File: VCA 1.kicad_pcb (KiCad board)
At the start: 2 copper layers, 171.3 x 128.5 mm, 87 parts, among them J1 Eurorack 2x8hs, J10 CV2, J11 IN2, J12 IN 1x8h, J13 OUT1, J14 OUT2, J15 IN 1x8s, J2 OUT 1x3s, J3 CV 1x9s, J5 CV 1x9h, J6 OUT 1x3h, J8 CV1, J9 IN1, Q1 2N3904, Q2 2N3904, U1 TL074, U2 AS2164

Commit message: Updated trim pot footprints
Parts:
- RV10, RV7, RV8, RV9: footprint Potentiometer_THT:Potentiometer_Bourns_3296W_Vertical -> Potentiometer_THT:Potentiometer_Bourns_3296X_Horizontal
- moved RV7 6.50 mm to (66.7, 55.6), turned to 180 degrees
- moved R16 5.02 mm to (55.1, 45.5), turned to 0 degrees
- moved RV8 3.52 mm to (66.7, 48.2), turned to 180 degrees
- moved RV10 2.66 mm to (62.2, 41.7), turned to -90 degrees
- moved RV9 0.50 mm to (54.0, 41.7), turned to -90 degrees
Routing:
- net Net-(R7-Pad1): track 4.29 -> 40.7 mm
- net Net-(R16-Pad1): track 5.23 -> 32.1 mm
- net -12v: track 185.4 -> 174.1 mm
- net Net-(R6-Pad1): track 4.33 -> 14.9 mm
- net Net-(R15-Pad1): track 4.98 -> 8.18 mm
- net GND: vias 9 -> 10
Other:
- board text added: "V 1.4"
- board text removed: "V 1.3"

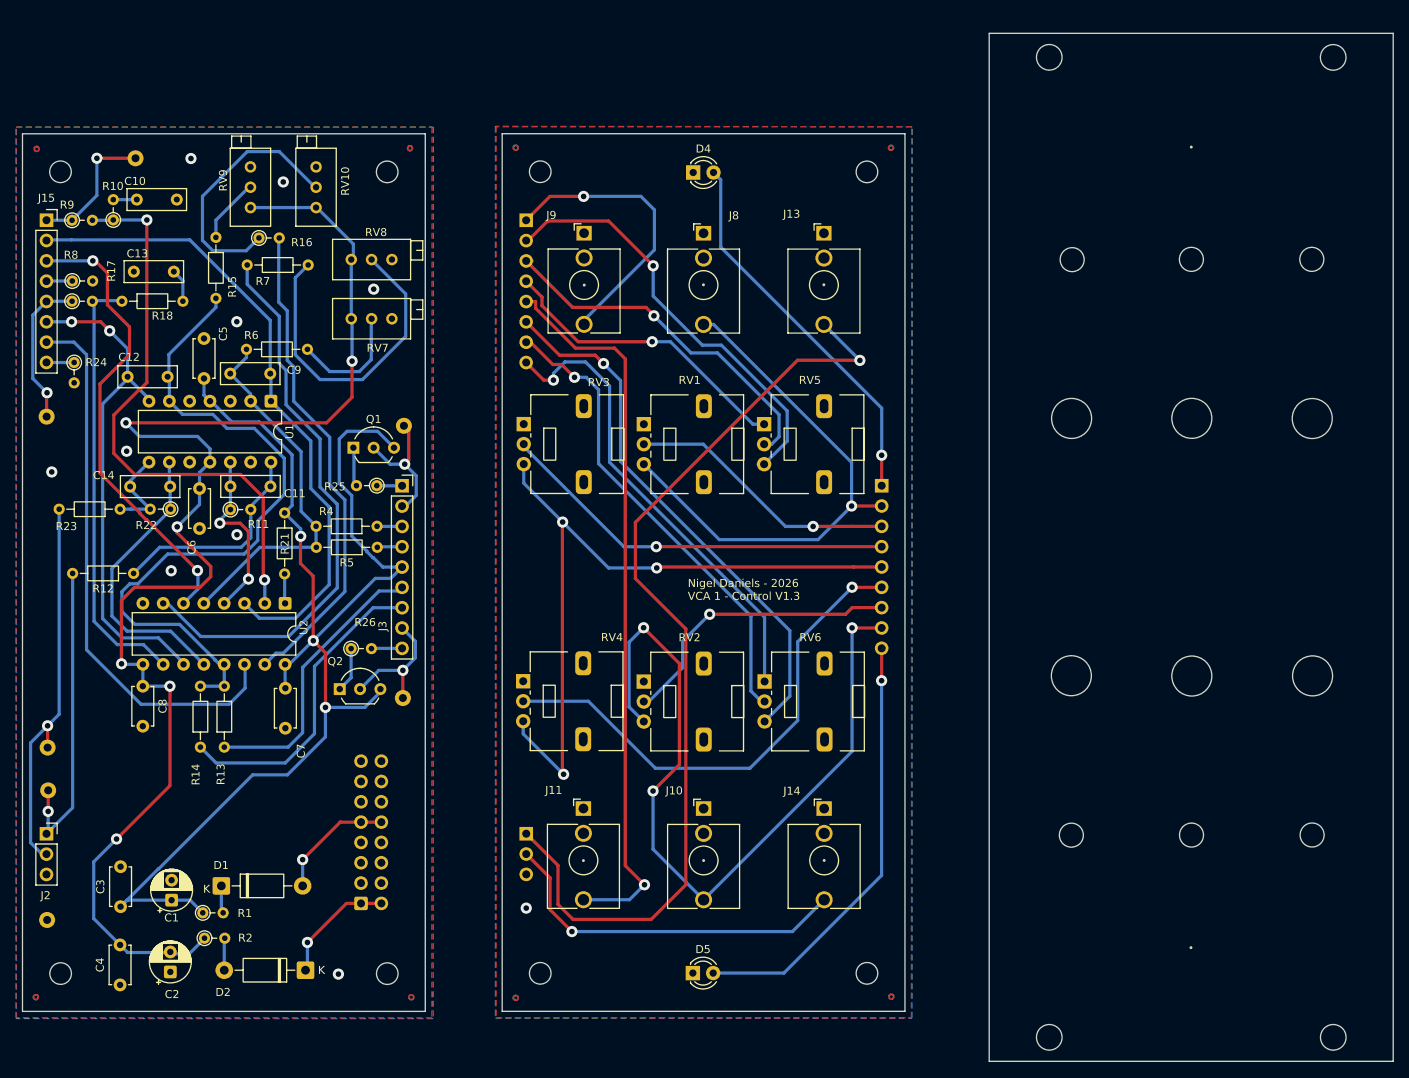
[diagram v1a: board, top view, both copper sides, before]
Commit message: Created custom AS2164 symbol, updated schematic, pcb and readme.
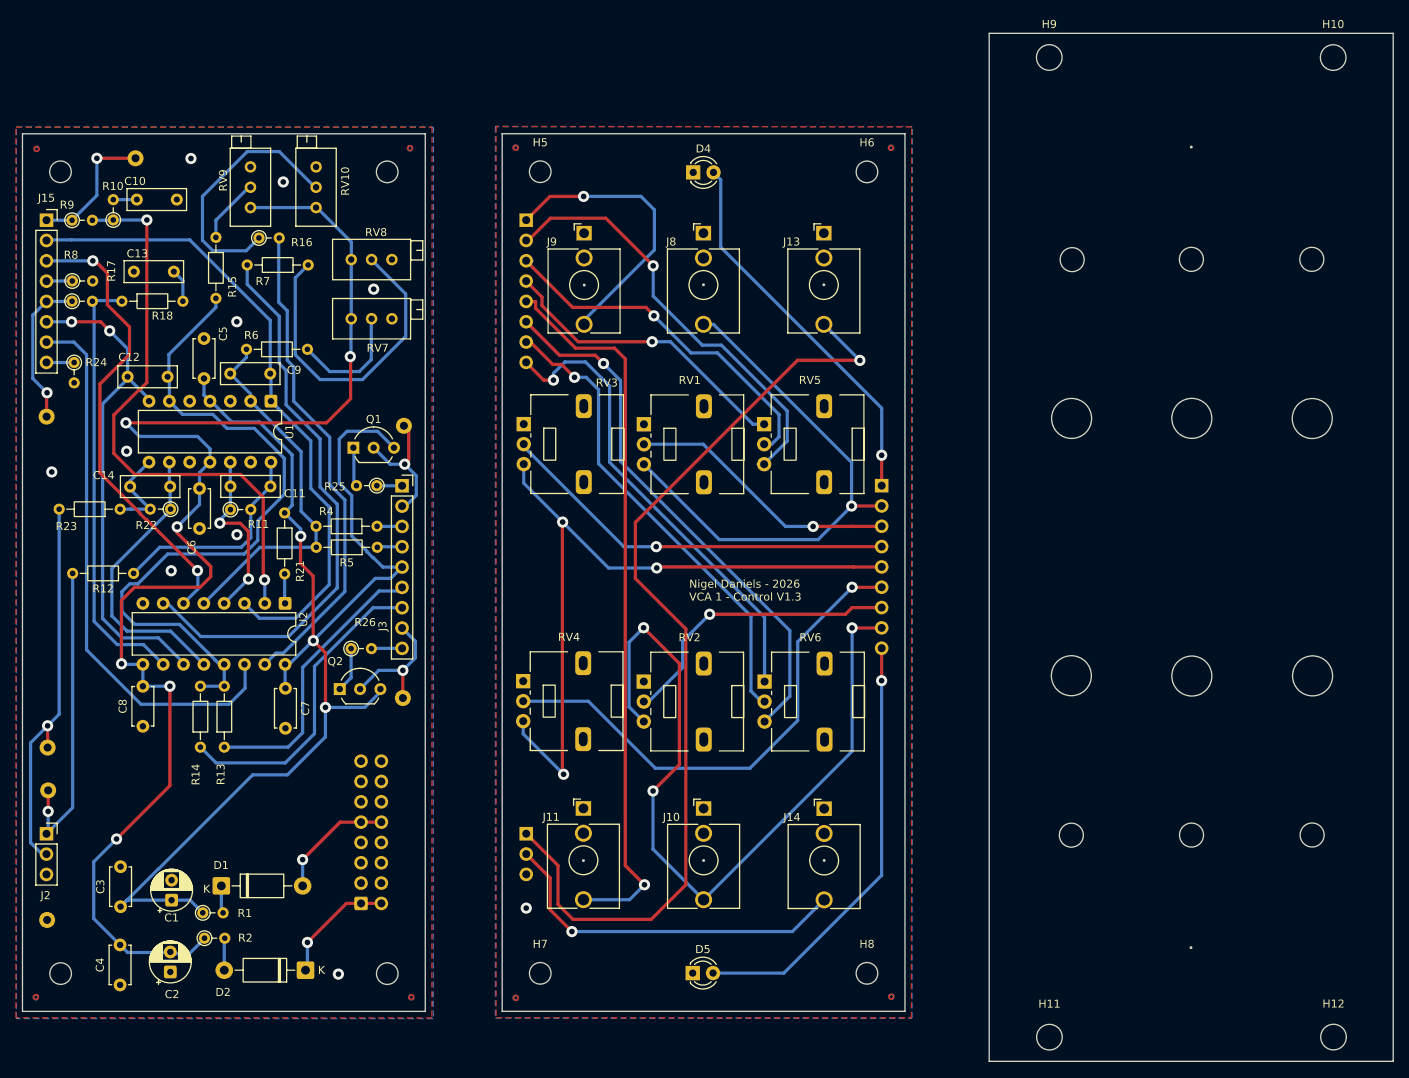
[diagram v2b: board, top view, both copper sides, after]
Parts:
- moved H7 40.8 mm to (90.3, 137.4)
- moved H8 40.8 mm to (131.1, 137.4)
- moved H12 35.5 mm to (189.4, 145.4)
- moved H11 35.5 mm to (153.9, 145.4)
- moved C8 5.01 mm to (40.6, 106.5), turned to 90 degrees
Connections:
- C8 pad 1: -12v -> GND
- C8 pad 2: GND -> -12v

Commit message: New simulation, updated design after breadboard test.
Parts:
- added R19: 390R, Resistor_THT:R_Axial_DIN0204_L3.6mm_D1.6mm_P2.54mm_Vertical, F.Cu at (34.4, 48.4)
- added R20: 390R, Resistor_THT:R_Axial_DIN0204_L3.6mm_D1.6mm_P2.54mm_Vertical, F.Cu at (53.3, 101.7)
- R24, R8: value 2K2 -> 3K3
- RV5, RV6: value 10K B -> 1K B
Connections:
- U2 pad 14: Net-(J15-Pin_7) -> Net-(U2D-CV)
- U2 pad 6: Net-(J15-Pin_3) -> Net-(U2B-CV)
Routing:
- net Net-(J15-Pin_3): track 58.4 -> 3.26 mm, vias 2 -> 0
- net Net-(U2B-CV): track 0.00 -> 54.5 mm, vias 0 -> 2
- net Net-(J15-Pin_7): track 69.0 -> 65.5 mm
- net Net-(U2D-CV): track 0.00 -> 3.03 mm

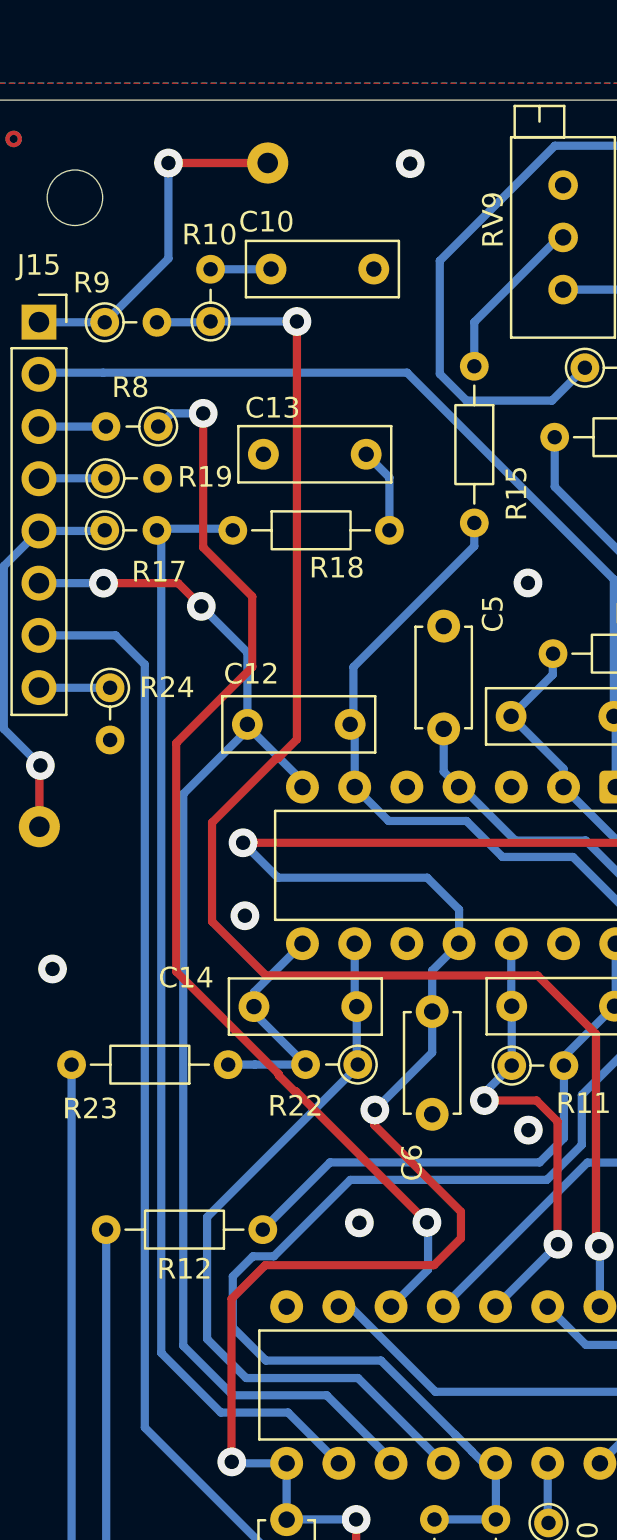
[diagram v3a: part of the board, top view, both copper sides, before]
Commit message: Updated curve values to match breadboard
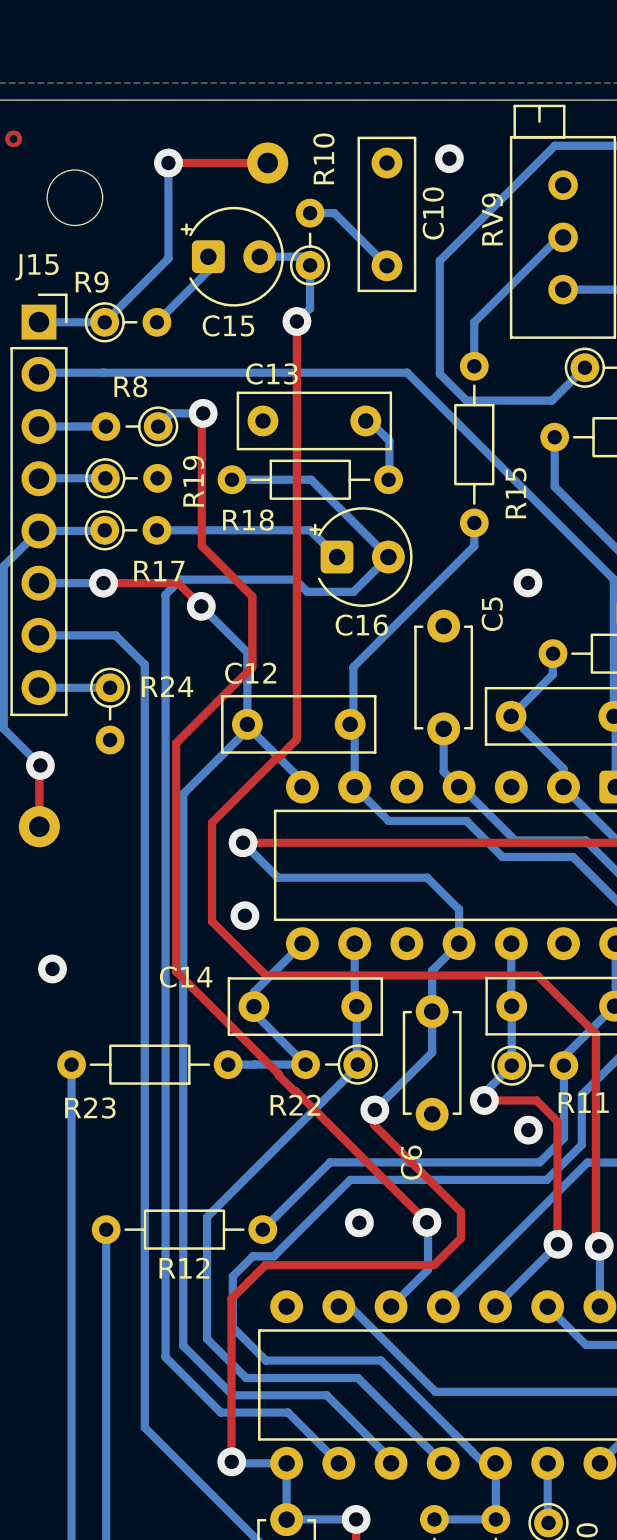
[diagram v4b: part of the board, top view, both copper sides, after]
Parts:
- added C15: 10uF t, Capacitor_THT:CP_Radial_Tantal_D4.5mm_P2.50mm, F.Cu at (36.8, 40.1)
- added C16: 10uF t, Capacitor_THT:CP_Radial_Tantal_D4.5mm_P2.50mm, F.Cu at (43.0, 54.7)
- R24, R8: value 3K3 -> 2K2
- RV5, RV6: value 1K B -> 10K B
- moved C10 5.64 mm to (45.5, 40.5), turned to 90 degrees
- moved R10 5.56 mm to (41.7, 40.5)
- moved R18 2.46 mm to (37.9, 50.9)
- moved C13 1.62 mm to (44.5, 48.1)
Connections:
- R17 pad 2: Net-(U2C-IN) -> Net-(C16-Pad1)
- R9 pad 2: Net-(U2A-IN) -> Net-(C15-Pad1)
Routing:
- net Net-(U2C-IN): track 54.7 -> 68.9 mm
- net Net-(C16-Pad1): track 0.00 -> 9.71 mm
- net Net-(C15-Pad1): track 0.00 -> 4.23 mm
- net Net-(C10-Pad1): track 2.94 -> 4.80 mm
- net Net-(U2A-IN): track 72.1 -> 70.9 mm
- net Net-(C13-Pad1): track 4.17 -> 3.46 mm

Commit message: Removed uneeded resistor
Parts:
- removed R19, R20: 390R, Resistor_THT:R_Axial_DIN0204_L3.6mm_D1.6mm_P2.54mm_Vertical
- R18: footprint Resistor_THT:R_Axial_DIN0204_L3.6mm_D1.6mm_P7.62mm_Horizontal -> Resistor_THT:R_Axial_DIN0204_L3.6mm_D1.6mm_P2.54mm_Vertical
- moved R18 9.21 mm to (47.1, 52.1), turned to 90 degrees
- moved C16 1.43 mm to (43.8, 53.5), turned to -90 degrees
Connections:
- U2 pad 14: Net-(U2D-CV) -> Net-(J15-Pin_7)
- U2 pad 6: Net-(U2B-CV) -> Net-(J15-Pin_3)
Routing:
- net Net-(J15-Pin_3): track 3.26 -> 59.3 mm, vias 0 -> 2
- net Net-(U2B-CV): track 54.6 -> 0.00 mm, vias 2 -> 0
- net Net-(U2C-IN): track 68.9 -> 62.3 mm
- net Net-(J15-Pin_7): track 65.5 -> 68.7 mm
- net Net-(U2D-CV): track 3.03 -> 0.00 mm

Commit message: Reworked R values for 0-8V CV
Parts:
- R15, R6: value 33K -> 10K
- R24, R8: value 2K2 -> 15K
- RV8: value 10K -> 20K
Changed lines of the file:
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@@
 			)
 		)
-		(property "Value" "2K2"
+		(property "Value" "15K"
 			(at -0.12 -1.77 0)
 			(layer "F.Fab")
@@
 			)
 		)
-		(property "Value" "33K"
+		(property "Value" "10K"
 			(at 1.78 -1.96 90)
 			(layer "F.Fab")
@@
 			)
 		)
-		(property "Value" "33K"
+		(property "Value" "10K"
 			(at 3.81 1.92 0)
 			(layer "F.Fab")
@@
 			)
 		)
-		(property "Value" "10K"
+		(property "Value" "20K"
 			(at -3.3 3.67 0)
 			(layer "F.Fab")
@@
 			)
 		)
-		(property "Value" "2K2"
+		(property "Value" "15K"
 			(at 1.53 -2.63 0)
 			(layer "F.Fab")
@@
 	)
 	(segment
-		(start 53.3 98.79)
-		(end 53.3 101.6)
-		(width 0.4)
-		(layer "B.Cu")
-		(net "Net-(J15-Pin_7)")
-	)
-	(segment
-		(start 53.3 98.79)
-		(end 53.38 98.87)
-		(width 0.4)
-		(layer "B.Cu")
-		(net "Net-(J15-Pin_7)")
-	)
-	(segment
-		(start 32.28 58.51)
-		(end 28.55 58.51)
-		(width 0.4)
-		(layer "B.Cu")
-		(net "Net-(J15-Pin_7)")
-	)
-	(segment
-		(start 53.3 101.6)
-		(end 51.54 103.36)
-		(width 0.4)
-		(layer "B.Cu")
-		(net "Net-(J15-Pin_7)")
-	)
-	(segment
-		(start 33.7 59.93)
-		(end 32.28 58.51)
-		(width 0.4)
-		(layer "B.Cu")
-		(net "Net-(J15-Pin_7)")
-	)
-	(segment
-		(start 33.7 97.05)
-		(end 33.7 59.93)
-		(width 0.4)
-		(layer "B.Cu")
-		(net "Net-(J15-Pin_7)")
-	)
-	(segment
-		(start 40.01 103.36)
-		(end 33.7 97.05)
-		(width 0.4)
-		(layer "B.Cu")
-		(net "Net-(J15-Pin_7)")
-	)
-	(segment
-		(start 51.54 103.36)
-		(end 40.01 103.36)
-		(width 0.4)
-		(layer "B.Cu")
-		(net "Net-(J15-Pin_7)")
-	)
-	(segment
 		(start 43.91 65.89)
 		(end 43.91 63.01)
@@
 	)
 	(segment
+		(start 53.3 98.79)
+		(end 53.3 101.6)
+		(width 0.4)
+		(layer "B.Cu")
+		(net "Net-(J15-Pin_7)")
+	)
+	(segment
+		(start 53.3 98.79)
+		(end 53.38 98.87)
+		(width 0.4)
+		(layer "B.Cu")
+		(net "Net-(J15-Pin_7)")
+	)
+	(segment
+		(start 32.28 58.51)
+		(end 28.55 58.51)
+		(width 0.4)
+		(layer "B.Cu")
+		(net "Net-(J15-Pin_7)")
+	)
+	(segment
+		(start 53.3 101.6)
+		(end 51.54 103.36)
+		(width 0.4)
+		(layer "B.Cu")
+		(net "Net-(J15-Pin_7)")
+	)
+	(segment
+		(start 33.7 59.93)
+		(end 32.28 58.51)
+		(width 0.4)
+		(layer "B.Cu")
+		(net "Net-(J15-Pin_7)")
+	)
+	(segment
+		(start 33.7 97.05)
+		(end 33.7 59.93)
+		(width 0.4)
+		(layer "B.Cu")
+		(net "Net-(J15-Pin_7)")
+	)
+	(segment
+		(start 40.01 103.36)
+		(end 33.7 97.05)
+		(width 0.4)
+		(layer "B.Cu")
+		(net "Net-(J15-Pin_7)")
+	)
+	(segment
+		(start 51.54 103.36)
+		(end 40.01 103.36)
+		(width 0.4)
+		(layer "B.Cu")
+		(net "Net-(J15-Pin_7)")
+	)
+	(segment

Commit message: Updated Curve to GND R
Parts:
- R24, R8: value 15K -> 10K
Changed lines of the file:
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@@
 			)
 		)
-		(property "Value" "15K"
+		(property "Value" "10K"
 			(at -0.12 -1.77 0)
 			(layer "F.Fab")
@@
 			)
 		)
-		(property "Value" "15K"
+		(property "Value" "10K"
 			(at 1.53 -2.63 0)
 			(layer "F.Fab")

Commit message: Returned Lin input RV to 10K
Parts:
- RV8: value 20K -> 10K
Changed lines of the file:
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@@
 			)
 		)
-		(property "Value" "20K"
+		(property "Value" "10K"
 			(at -3.3 3.67 0)
 			(layer "F.Fab")
